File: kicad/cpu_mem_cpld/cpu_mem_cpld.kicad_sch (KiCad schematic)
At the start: 46 parts, among them CON1 BARREL_JACK, J1 USB, J3 DB9, SW1 SW_PUSH, U1 W65C02, U10 74HCT245, U11 16550, U13 MAX232, U2 CHUCK, U3 28C256, U4 AS6C4008, U5 74LS06, U6 LM555N, U9 74HCT245, X1 OSC, X2 OSC

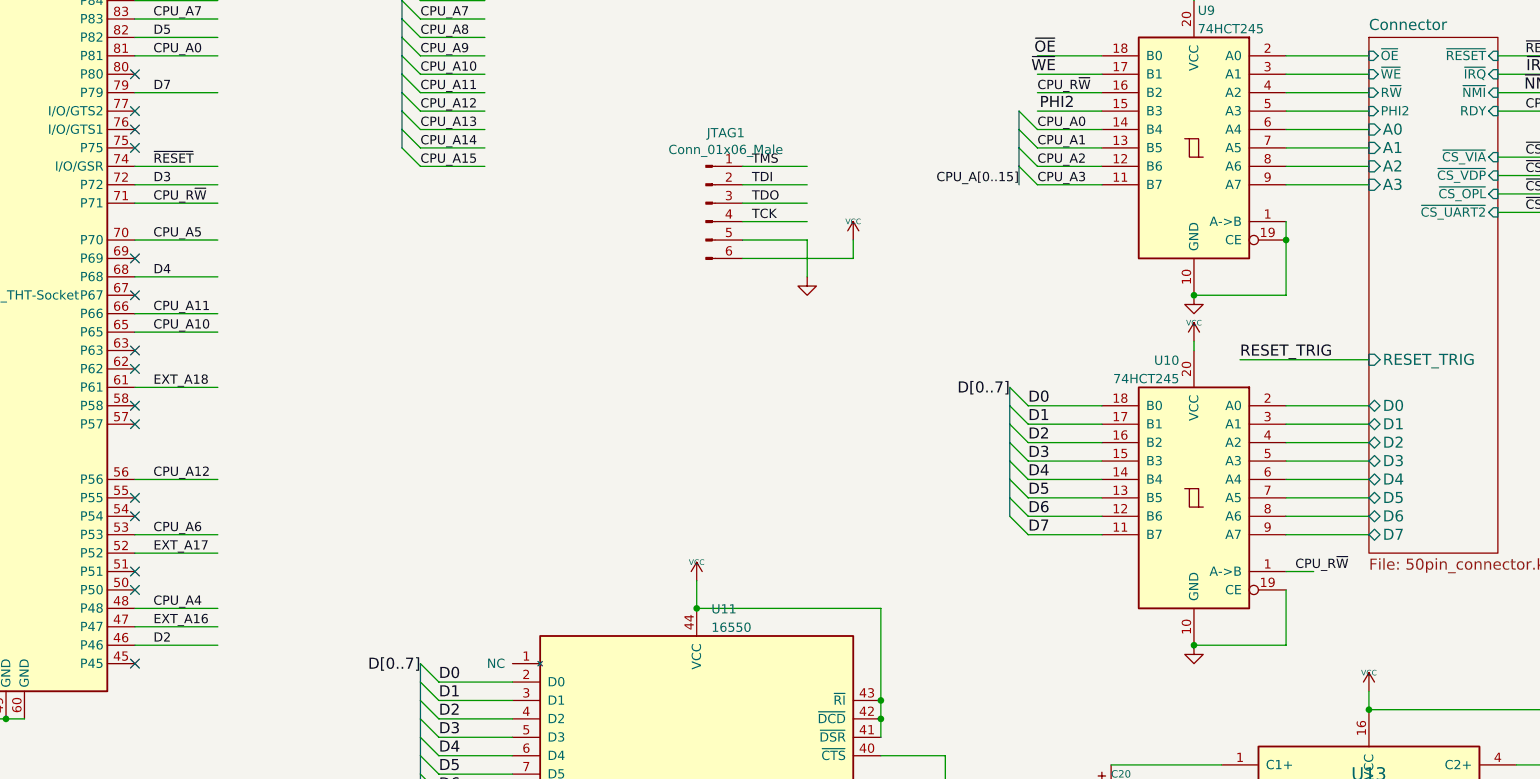
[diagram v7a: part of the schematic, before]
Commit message: cs line for data bus buffer
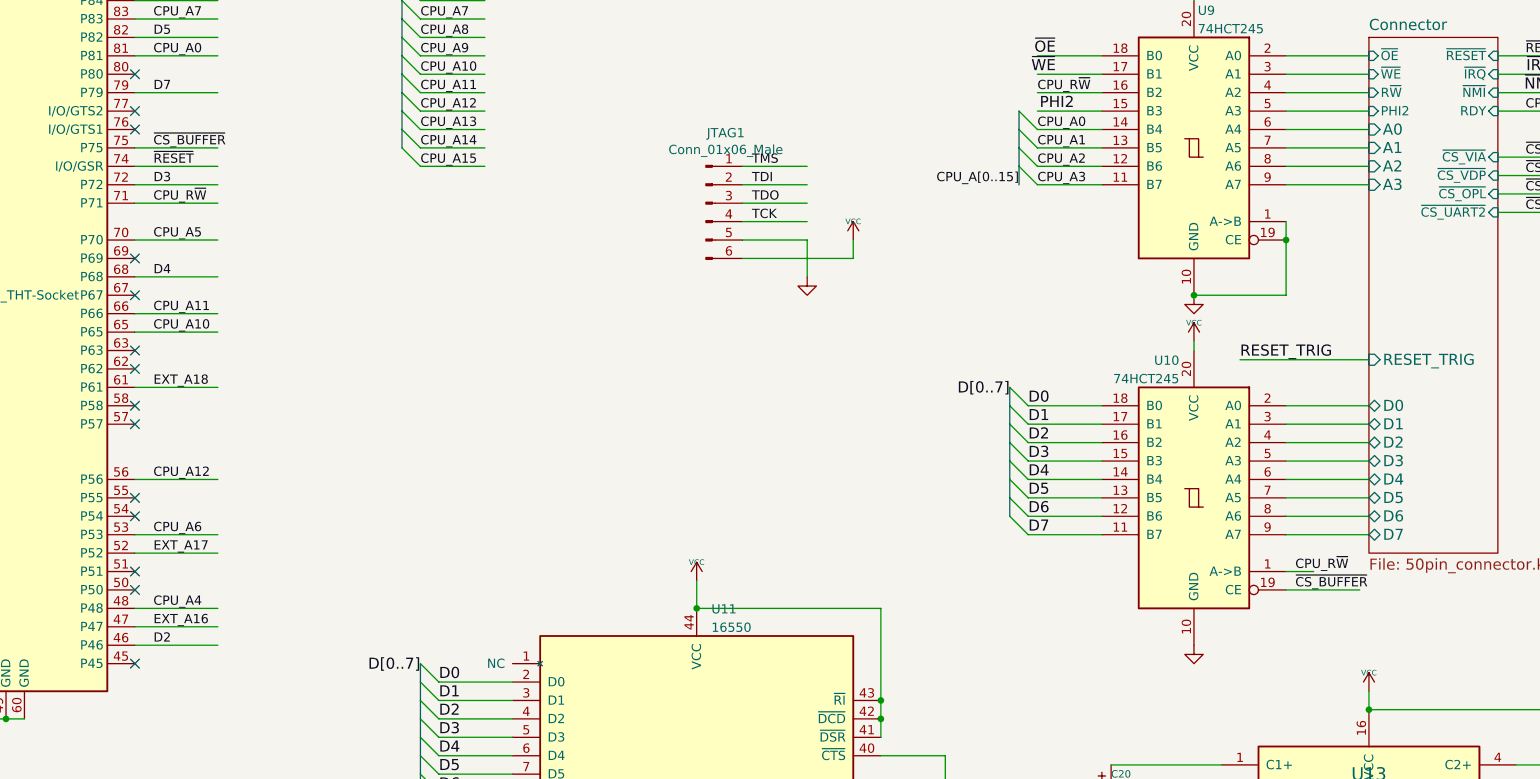
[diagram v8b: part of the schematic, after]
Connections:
- net GND: no longer U10.19 (CE)
- net ~{CS_BUFFER}: now reaches U2.75 (P75)
- net ~{CS_BUFFER}: now also U10.19 (CE)
- no-connect marks 52 -> 51
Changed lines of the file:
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@@
   (junction (at 114.3 250.19) (diameter 0) (color 0 0 0 0)
-  )
-  (junction (at 342.9 130.81) (diameter 0) (color 0 0 0 0)
   )
   (junction (at 246.38 194.31) (diameter 0) (color 0 0 0 0)
@@
   (no_connect (at 196.85 59.69))
   (no_connect (at 196.85 57.15))
-  (no_connect (at 196.85 62.23))
   (no_connect (at 196.85 77.47))
   (no_connect (at 400.05 229.87))
@@
     (stroke (width 0) (type default) (color 0 0 0 0))
   )
+  (wire (pts (xy 196.85 62.23) (xy 208.28 62.23))
+    (stroke (width 0) (type default) (color 0 0 0 0))
+  )
   (wire (pts (xy 20.32 34.29) (xy 30.48 34.29))
     (stroke (width 0) (type default) (color 0 0 0 0))
@@
     (stroke (width 0) (type default) (color 0 0 0 0))
   )
-  (wire (pts (xy 355.6 130.81) (xy 342.9 130.81))
-    (stroke (width 0) (type default) (color 0 0 0 0))
-  )
   (bus (pts (xy 281.94 24.13) (xy 281.94 26.67))
     (stroke (width 0) (type default) (color 0 0 0 0))
@@
     (stroke (width 0) (type default) (color 0 0 0 0))
   )
+  (wire (pts (xy 355.6 123.19) (xy 365.76 123.19))
+    (stroke (width 0) (type default) (color 0 0 0 0))
+  )
   (wire (pts (xy 245.11 49.53) (xy 236.22 49.53))
     (stroke (width 0) (type default) (color 0 0 0 0))
@@
   )
   (wire (pts (xy 387.35 187.96) (xy 387.35 229.87))
-    (stroke (width 0) (type default) (color 0 0 0 0))
-  )
-  (wire (pts (xy 355.6 123.19) (xy 355.6 130.81))
     (stroke (width 0) (type default) (color 0 0 0 0))
   )
@@
     (effects (font (size 1.27 1.27)) (justify left bottom))
   )
+  (label "~{CS_BUFFER}" (at 199.39 62.23 0)
+    (effects (font (size 1.27 1.27)) (justify left bottom))
+  )
   (label "D1" (at 83.82 166.37 0)
     (effects (font (size 1.524 1.524)) (justify left bottom))
@@
     (effects (font (size 1.27 1.27)) (justify left bottom))
   )
+  (label "~{CS_BUFFER}" (at 356.87 123.19 0)
+    (effects (font (size 1.27 1.27)) (justify left bottom))
+  )
